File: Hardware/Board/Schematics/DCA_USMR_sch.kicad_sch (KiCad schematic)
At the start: 22 parts, among them J1 Conn_02x03_Counter_Clockwise, J3 Barrel_Jack_Switch, U1 ATSAMD20E18, U2 LD1117S33TR_SOT223

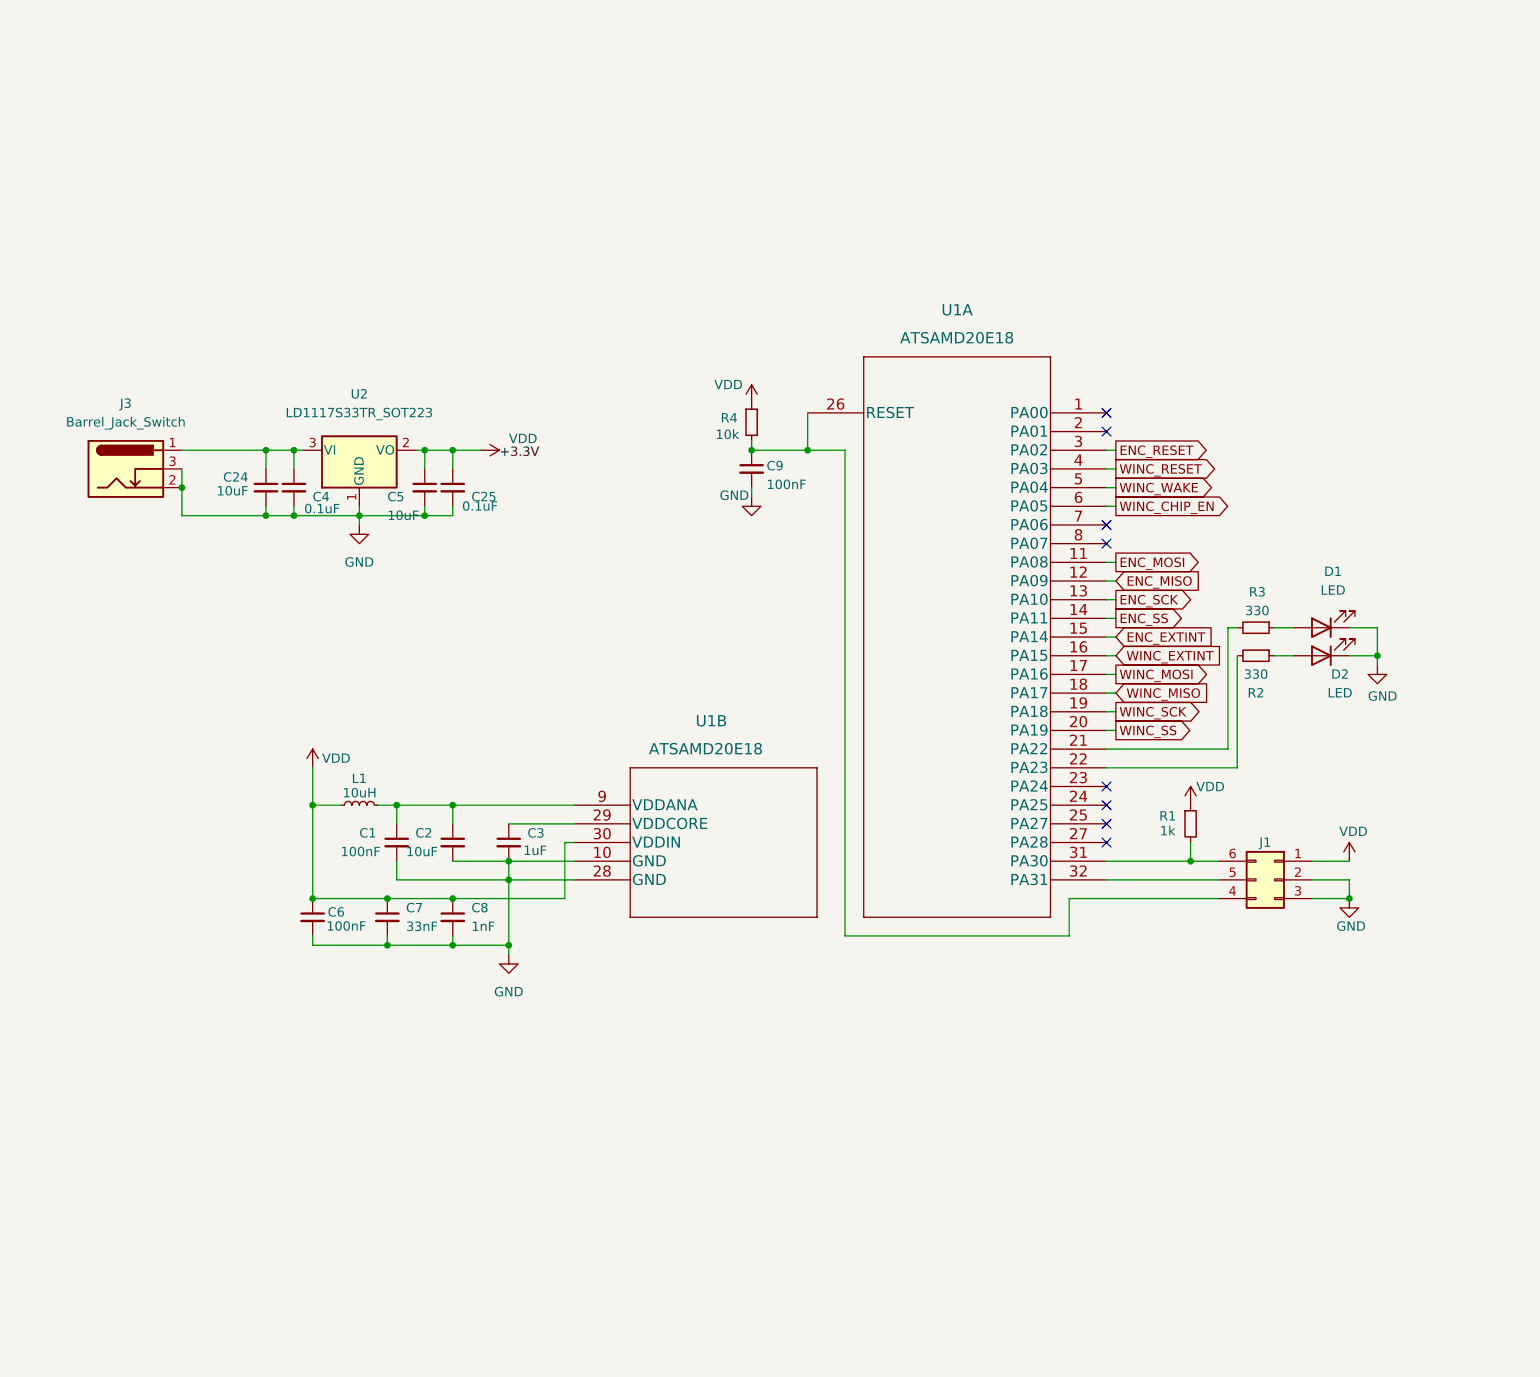
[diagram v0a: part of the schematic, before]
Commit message: Newest board spin. Fixed Wifi, and ethernet SPI ports. Added Sensor connectors with digital In/Outs
Signed-off-by: Darren <Darmor>
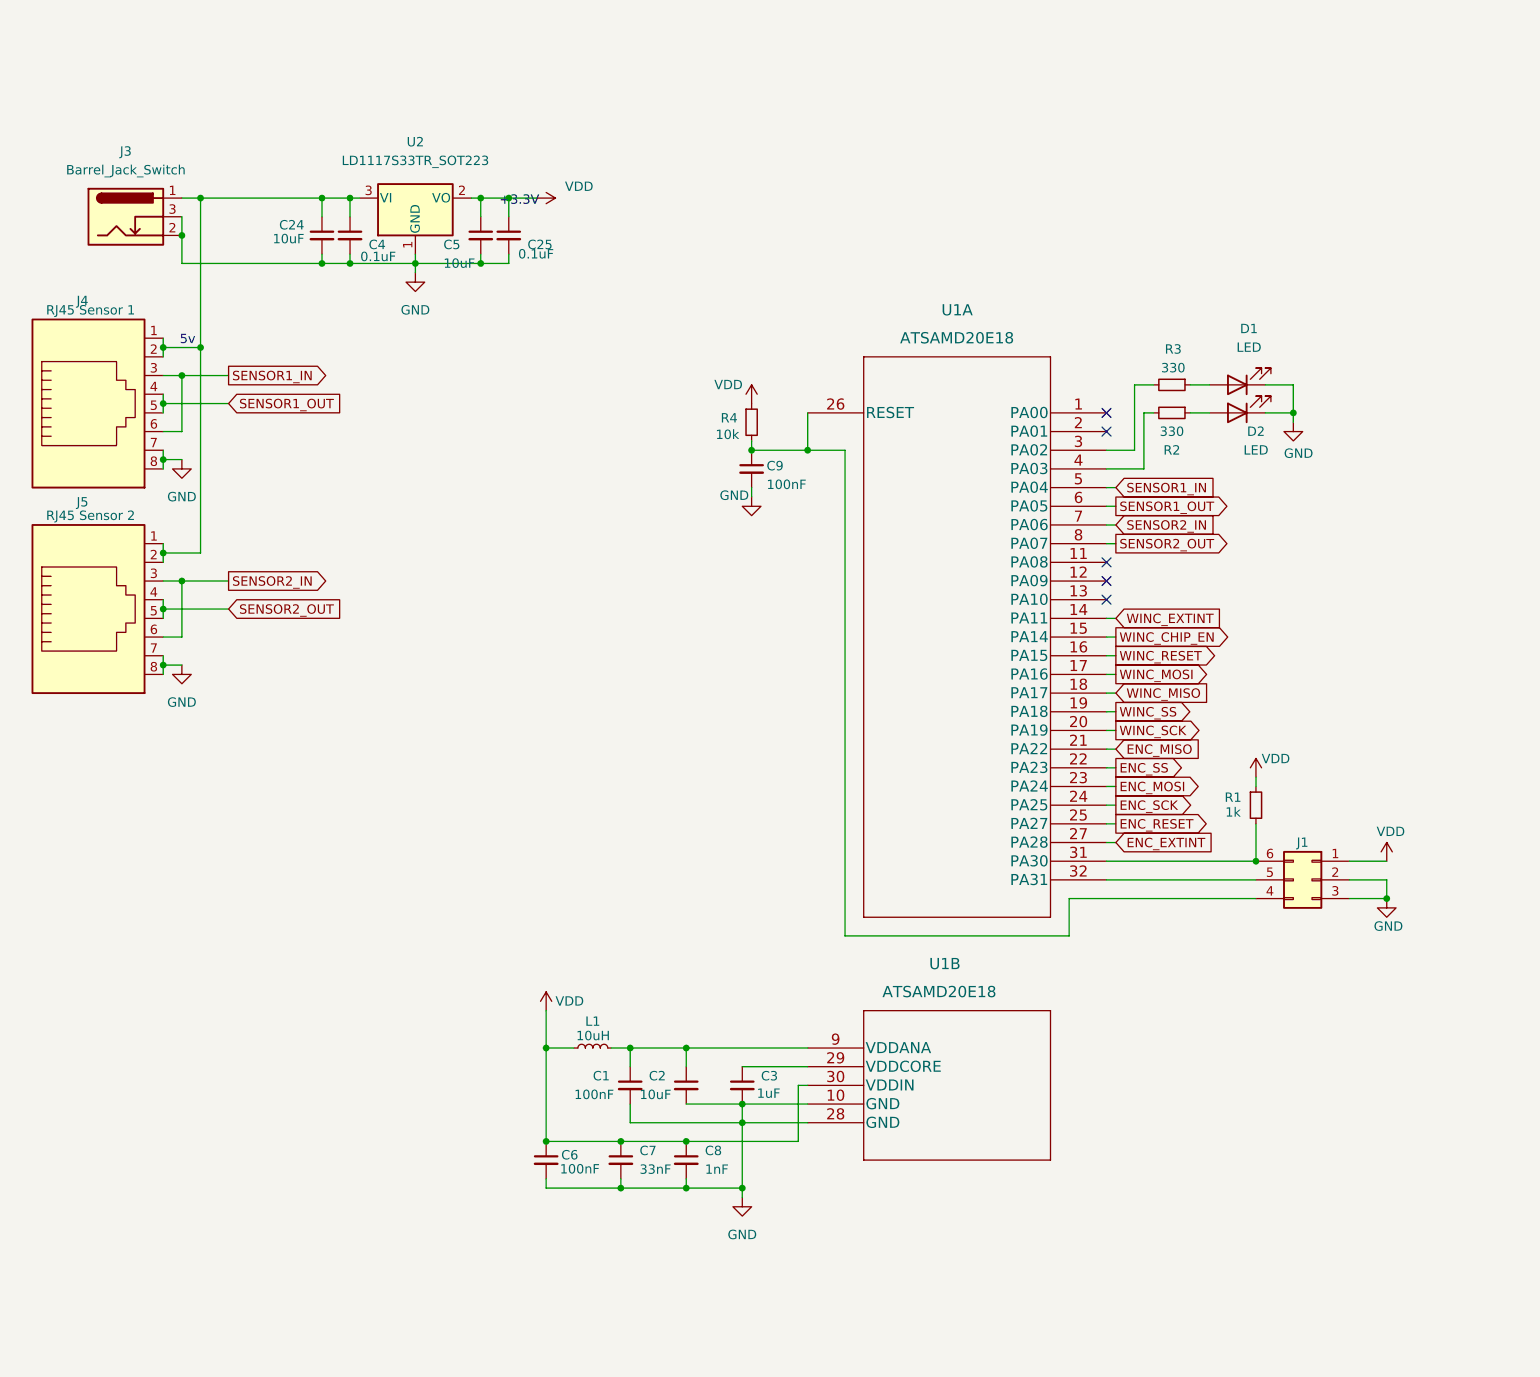
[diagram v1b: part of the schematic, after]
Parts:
- added J4: RJ45 Sensor 1, Connector_RJ:RJ45_Plug_Metz_AJP92A8813, symbol Connector:RJ45
- added J5: RJ45 Sensor 2, Connector_RJ:RJ45_Plug_Metz_AJP92A8813, symbol Connector:RJ45
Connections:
- net ENC_EXTINT: now also U1.27 (PA28); no longer U1.15 (PA14)
- net ENC_MISO: now also U1.21 (PA22); no longer U1.12 (PA09)
- net ENC_MOSI: now also U1.23 (PA24); no longer U1.11 (PA08)
- net ENC_RESET: now also U1.25 (PA27); no longer U1.3 (PA02)
- net ENC_SCK: now also U1.24 (PA25); no longer U1.13 (PA10)
- net ENC_SS: now also U1.22 (PA23); no longer U1.14 (PA11)
- net GND: now also J4.7, J4.8, J5.7, J5.8
- net WINC_CHIP_EN: now also U1.15 (PA14); no longer U1.6 (PA05)
- net WINC_EXTINT: now also U1.14 (PA11); no longer U1.16 (PA15)
- net WINC_RESET: now also U1.16 (PA15); no longer U1.4 (PA03)
- net WINC_SCK: now also U1.20 (PA19); no longer U1.19 (PA18)
- net WINC_SS: now also U1.19 (PA18); no longer U1.20 (PA19)
- net at R3.2: now also U1.3 (PA02); no longer U1.21 (PA22)
- net at R2.2: now also U1.4 (PA03); no longer U1.22 (PA23)
- net SENSOR2_IN: now reaches U1.7 (PA06)
- net SENSOR2_IN: now also J5.3, J5.6
- net SENSOR2_OUT: now reaches U1.8 (PA07)
- net SENSOR2_OUT: now also J5.4, J5.5
- net at C24.1, C4.1, J3.1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: now also J4.1, J4.2, J5.1, J5.2
- net WINC_WAKE renamed SENSOR1_IN
- net SENSOR1_IN: now also J4.3, J4.6
- new net SENSOR1_OUT: J4.4, J4.5, U1.6 (PA05)
- no-connect marks 8 -> 5
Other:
- note added: "5v"
- moved on the sheet: C1, C2, C24, C25, C3, C4, C5, C6, C7, C8, D1, D2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
